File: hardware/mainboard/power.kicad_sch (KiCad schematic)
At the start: 18 parts, among them J1 Eurorack Power, U1 LD1117-3.3, U2 LM4040DBZ-10

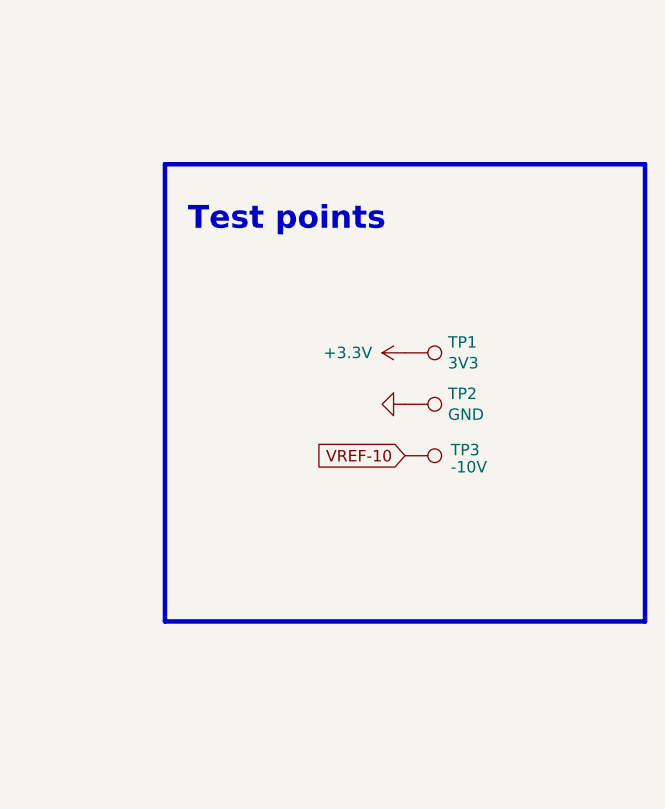
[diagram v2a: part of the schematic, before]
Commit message: A little more schematic cleanup
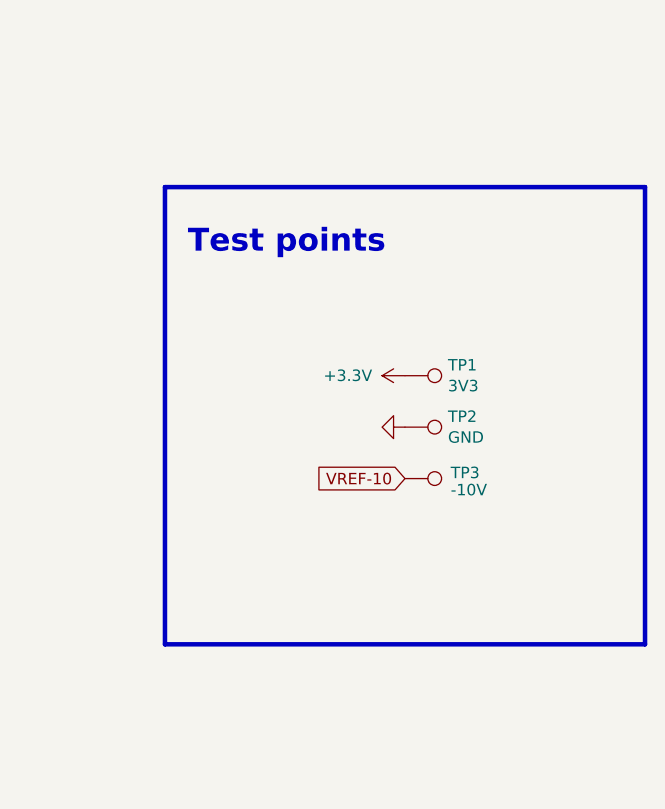
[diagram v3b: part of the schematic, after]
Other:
- moved on the sheet: TP1, TP2, TP3
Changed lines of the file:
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@@
     (stroke (width 0) (type default) (color 0 0 0 0))
   )
-  (polyline (pts (xy 208.28 114.3) (xy 208.28 165.1))
+  (polyline (pts (xy 208.28 116.84) (xy 208.28 167.64))
     (stroke (width 0.5) (type solid) (color 0 0 0 0))
   )
@@
     (stroke (width 0) (type default) (color 0 0 0 0))
   )
-  (polyline (pts (xy 208.28 165.1) (xy 261.62 165.1))
+  (polyline (pts (xy 208.28 167.64) (xy 261.62 167.64))
     (stroke (width 0.5) (type solid) (color 0 0 0 0))
   )
@@
     (stroke (width 0) (type default) (color 0 0 0 0))
   )
-  (polyline (pts (xy 208.28 114.3) (xy 261.62 114.3))
+  (polyline (pts (xy 208.28 116.84) (xy 261.62 116.84))
     (stroke (width 0.5) (type solid) (color 0 0 0 0))
   )
@@
     (stroke (width 0.5) (type solid) (color 0 0 0 0))
   )
-  (polyline (pts (xy 261.62 165.1) (xy 261.62 114.3))
+  (polyline (pts (xy 261.62 167.64) (xy 261.62 116.84))
     (stroke (width 0.5) (type solid) (color 0 0 0 0))
   )
@@
     (effects (font (size 2.54 2.54) (thickness 0.508) bold) (justify left bottom))
   )
-  (text "Test points" (at 210.82 121.92 0)
+  (text "Test points" (at 210.82 124.46 0)
     (effects (font (size 2.54 2.54) (thickness 0.508) bold) (justify left bottom))
   )
@@
     )
   )
-  (global_label "VREF-10" (shape input) (at 234.95 146.685 180) (fields_autoplaced)
+  (global_label "VREF-10" (shape input) (at 234.95 149.225 180) (fields_autoplaced)
     (effects (font (size 1.27 1.27)) (justify right))
-    (property "Intersheet References" "${INTERSHEET_REFS}" (id 0) (at 307.34 225.425 0)
+    (property "Intersheet References" "${INTERSHEET_REFS}" (id 0) (at 307.34 227.965 0)
       (effects (font (size 1.27 1.27)) hide)
     )
@@
     (pin "1")
   )
-  (symbol (lib_id "power:GND") (at 234.95 140.97 270) (unit 1)
-    (in_bom yes) (on_board yes)
-    (property "Reference" "#PWR013" (id 0) (at 228.6 140.97 0)
-      (effects (font (size 1.27 1.27)) hide)
-    )
-    (property "Value" "GND" (id 1) (at 230.5558 141.097 0)
-      (effects (font (size 1.27 1.27)) hide)
-    )
-    (property "Footprint" "" (id 2) (at 234.95 140.97 0)
-      (effects (font (size 1.27 1.27)) hide)
-    )
-    (property "Datasheet" "" (id 3) (at 234.95 140.97 0)
-      (effects (font (size 1.27 1.27)) hide)
-    )
-    (pin "1")
-  )
-  (symbol (lib_id "power:+3.3V") (at 234.95 135.255 90) (unit 1)
-    (in_bom yes) (on_board yes)
-    (property "Reference" "#PWR012" (id 0) (at 238.76 135.255 0)
-      (effects (font (size 1.27 1.27)) hide)
-    )
-    (property "Value" "+3.3V" (id 1) (at 228.6 135.255 90))
-    (property "Footprint" "" (id 2) (at 234.95 135.255 0)
-      (effects (font (size 1.27 1.27)) hide)
-    )
-    (property "Datasheet" "" (id 3) (at 234.95 135.255 0)
+  (symbol (lib_id "power:GND") (at 234.95 143.51 270) (unit 1)
+    (in_bom yes) (on_board yes)
+    (property "Reference" "#PWR013" (id 0) (at 228.6 143.51 0)
+      (effects (font (size 1.27 1.27)) hide)
+    )
+    (property "Value" "GND" (id 1) (at 230.5558 143.637 0)
+      (effects (font (size 1.27 1.27)) hide)
+    )
+    (property "Footprint" "" (id 2) (at 234.95 143.51 0)
+      (effects (font (size 1.27 1.27)) hide)
+    )
+    (property "Datasheet" "" (id 3) (at 234.95 143.51 0)
+      (effects (font (size 1.27 1.27)) hide)
+    )
+    (pin "1")
+  )
+  (symbol (lib_id "power:+3.3V") (at 234.95 137.795 90) (unit 1)
+    (in_bom yes) (on_board yes)
+    (property "Reference" "#PWR012" (id 0) (at 238.76 137.795 0)
+      (effects (font (size 1.27 1.27)) hide)
+    )
+    (property "Value" "+3.3V" (id 1) (at 228.6 137.795 90))
+    (property "Footprint" "" (id 2) (at 234.95 137.795 0)
+      (effects (font (size 1.27 1.27)) hide)
+    )
+    (property "Datasheet" "" (id 3) (at 234.95 137.795 0)
       (effects (font (size 1.27 1.27)) hide)
     )
@@
     (pin "1")
   )
-  (symbol (lib_id "Connector:TestPoint") (at 234.95 146.685 270) (unit 1)
-    (in_bom yes) (on_board yes)
-    (property "Reference" "TP3" (id 0) (at 240.03 146.05 90)
-      (effects (font (size 1.27 1.27)) (justify left))
-    )
-    (property "Value" "-10V" (id 1) (at 240.03 147.955 90)
-      (effects (font (size 1.27 1.27)) (justify left))
-    )
-    (property "Footprint" "TestPoint:TestPoint_Pad_D1.0mm" (id 2) (at 234.95 151.765 0)
-      (effects (font (size 1.27 1.27)) hide)
-    )
-    (property "Datasheet" "~" (id 3) (at 234.95 151.765 0)
-      (effects (font (size 1.27 1.27)) hide)
-    )
-    (property "dnp" "1" (id 4) (at 234.95 146.685 0)
-      (effects (font (size 1.27 1.27)) hide)
-    )
-    (property "finalized" "n/a" (id 5) (at 234.95 146.685 0)
-      (effects (font (size 1.27 1.27)) hide)
-    )
-    (pin "1")
-  )
-  (symbol (lib_id "Connector:TestPoint") (at 234.95 135.255 270) (unit 1)
-    (in_bom yes) (on_board yes)
-    (property "Reference" "TP1" (id 0) (at 239.7252 134.0866 90)
-      (effects (font (size 1.27 1.27)) (justify left))
-    )
-    (property "Value" "3V3" (id 1) (at 239.7252 136.398 90)
-      (effects (font (size 1.27 1.27)) (justify left))
-    )
-    (property "Footprint" "TestPoint:TestPoint_Pad_D1.0mm" (id 2) (at 234.95 140.335 0)
-      (effects (font (size 1.27 1.27)) hide)
-    )
-    (property "Datasheet" "~" (id 3) (at 234.95 140.335 0)
-      (effects (font (size 1.27 1.27)) hide)
-    )
-    (property "dnp" "1" (id 4) (at 234.95 135.255 0)
-      (effects (font (size 1.27 1.27)) hide)
-    )
-    (property "finalized" "n/a" (id 5) (at 234.95 135.255 0)
+  (symbol (lib_id "Connector:TestPoint") (at 234.95 149.225 270) (unit 1)
+    (in_bom yes) (on_board yes)
+    (property "Reference" "TP3" (id 0) (at 240.03 148.59 90)
+      (effects (font (size 1.27 1.27)) (justify left))
+    )
+    (property "Value" "-10V" (id 1) (at 240.03 150.495 90)
+      (effects (font (size 1.27 1.27)) (justify left))
+    )
+    (property "Footprint" "TestPoint:TestPoint_Pad_D1.0mm" (id 2) (at 234.95 154.305 0)
+      (effects (font (size 1.27 1.27)) hide)
+    )
+    (property "Datasheet" "~" (id 3) (at 234.95 154.305 0)
+      (effects (font (size 1.27 1.27)) hide)
+    )
+    (property "dnp" "1" (id 4) (at 234.95 149.225 0)
+      (effects (font (size 1.27 1.27)) hide)
+    )
+    (property "finalized" "n/a" (id 5) (at 234.95 149.225 0)
+      (effects (font (size 1.27 1.27)) hide)
+    )
+    (pin "1")
+  )
+  (symbol (lib_id "Connector:TestPoint") (at 234.95 137.795 270) (unit 1)
+    (in_bom yes) (on_board yes)
+    (property "Reference" "TP1" (id 0) (at 239.7252 136.6266 90)
+      (effects (font (size 1.27 1.27)) (justify left))
+    )
+    (property "Value" "3V3" (id 1) (at 239.7252 138.938 90)
+      (effects (font (size 1.27 1.27)) (justify left))
+    )
+    (property "Footprint" "TestPoint:TestPoint_Pad_D1.0mm" (id 2) (at 234.95 142.875 0)
+      (effects (font (size 1.27 1.27)) hide)
+    )
+    (property "Datasheet" "~" (id 3) (at 234.95 142.875 0)
+      (effects (font (size 1.27 1.27)) hide)
+    )
+    (property "dnp" "1" (id 4) (at 234.95 137.795 0)
+      (effects (font (size 1.27 1.27)) hide)
+    )
+    (property "finalized" "n/a" (id 5) (at 234.95 137.795 0)
       (effects (font (size 1.27 1.27)) hide)
     )
@@
     (pin "2")
   )
-  (symbol (lib_id "Connector:TestPoint") (at 234.95 140.97 270) (unit 1)
-    (in_bom yes) (on_board yes)
-    (property "Reference" "TP2" (id 0) (at 239.7252 139.8016 90)
-      (effects (font (size 1.27 1.27)) (justify left))
-    )
-    (property "Value" "GND" (id 1) (at 239.7252 142.113 90)
-      (effects (font (size 1.27 1.27)) (justify left))
-    )
-    (property "Footprint" "TestPoint:TestPoint_Pad_D1.0mm" (id 2) (at 234.95 146.05 0)
-      (effects (font (size 1.27 1.27)) hide)
-    )
-    (property "Datasheet" "~" (id 3) (at 234.95 146.05 0)
-      (effects (font (size 1.27 1.27)) hide)
-    )
-    (property "dnp" "1" (id 4) (at 234.95 140.97 0)
-      (effects (font (size 1.27 1.27)) hide)
-    )
-    (property "finalized" "n/a" (id 5) (at 234.95 140.97 0)
-      (effects (font (size 1.27 1.27)) hide)
-    )
+  (symbol (lib_id "Connector:TestPoint") (at 234.95 143.51 270) (unit 1)
+    (in_bom yes) (on_board yes)
+    (property "Reference" "TP2" (id 0) (at 239.7252 142.3416 90)
+      (effects (font (size 1.27 1.27)) (justify left))
+    )
+    (property "Value" "GND" (id 1) (at 239.7252 144.653 90)
+      (effects (font (size 1.27 1.27)) (justify left))
+    )
+    (property "Footprint" "TestPoint:TestPoint_Pad_D1.0mm" (id 2) (at 234.95 148.59 0)
+      (effects (font (size 1.27 1.27)) hide)
+    )
+    (property "Datasheet" "~" (id 3) (at 234.95 148.59 0)
+      (effects (font (size 1.27 1.27)) hide)
+    )
+    (property "dnp" "1" (id 4) (at 234.95 143.51 0)
+      (effects (font (size 1.27 1.27)) hide)
+    )
+    (property "finalized" "n/a" (id 5) (at 234.95 143.51 0)
+      (effects (font (size 1.27 1.27)) hide)
+    )

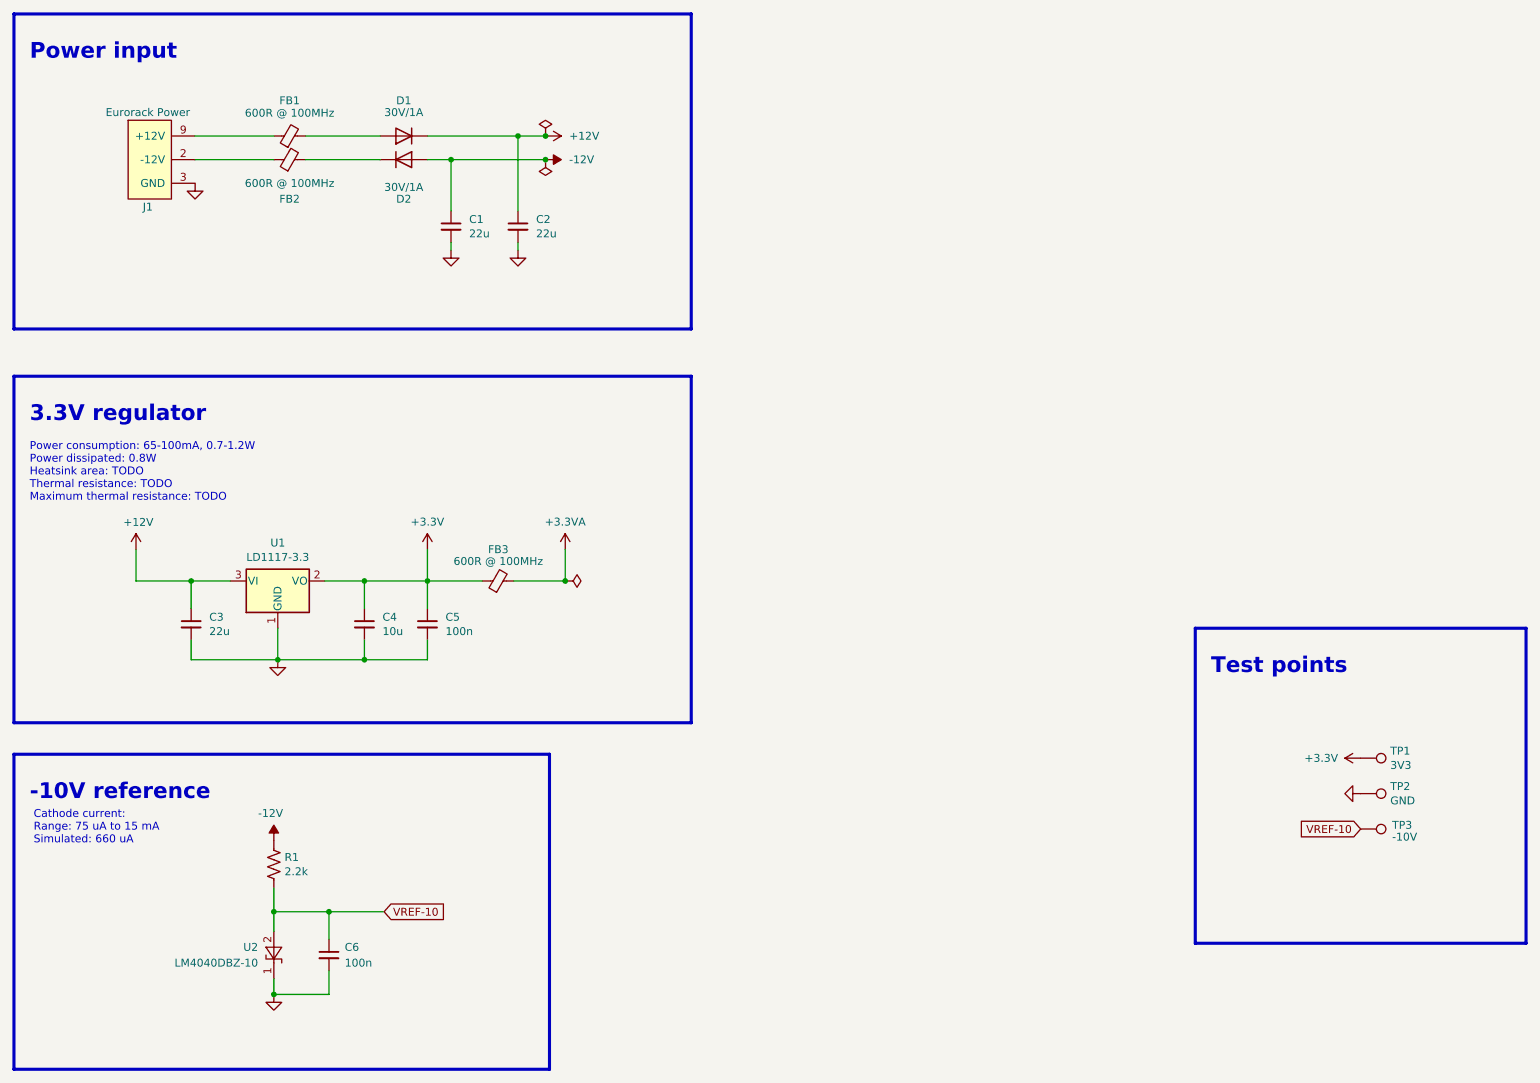
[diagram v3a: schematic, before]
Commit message: * Added versions strapping pins * Added VBUS power * Filled out regulator thermal calculations
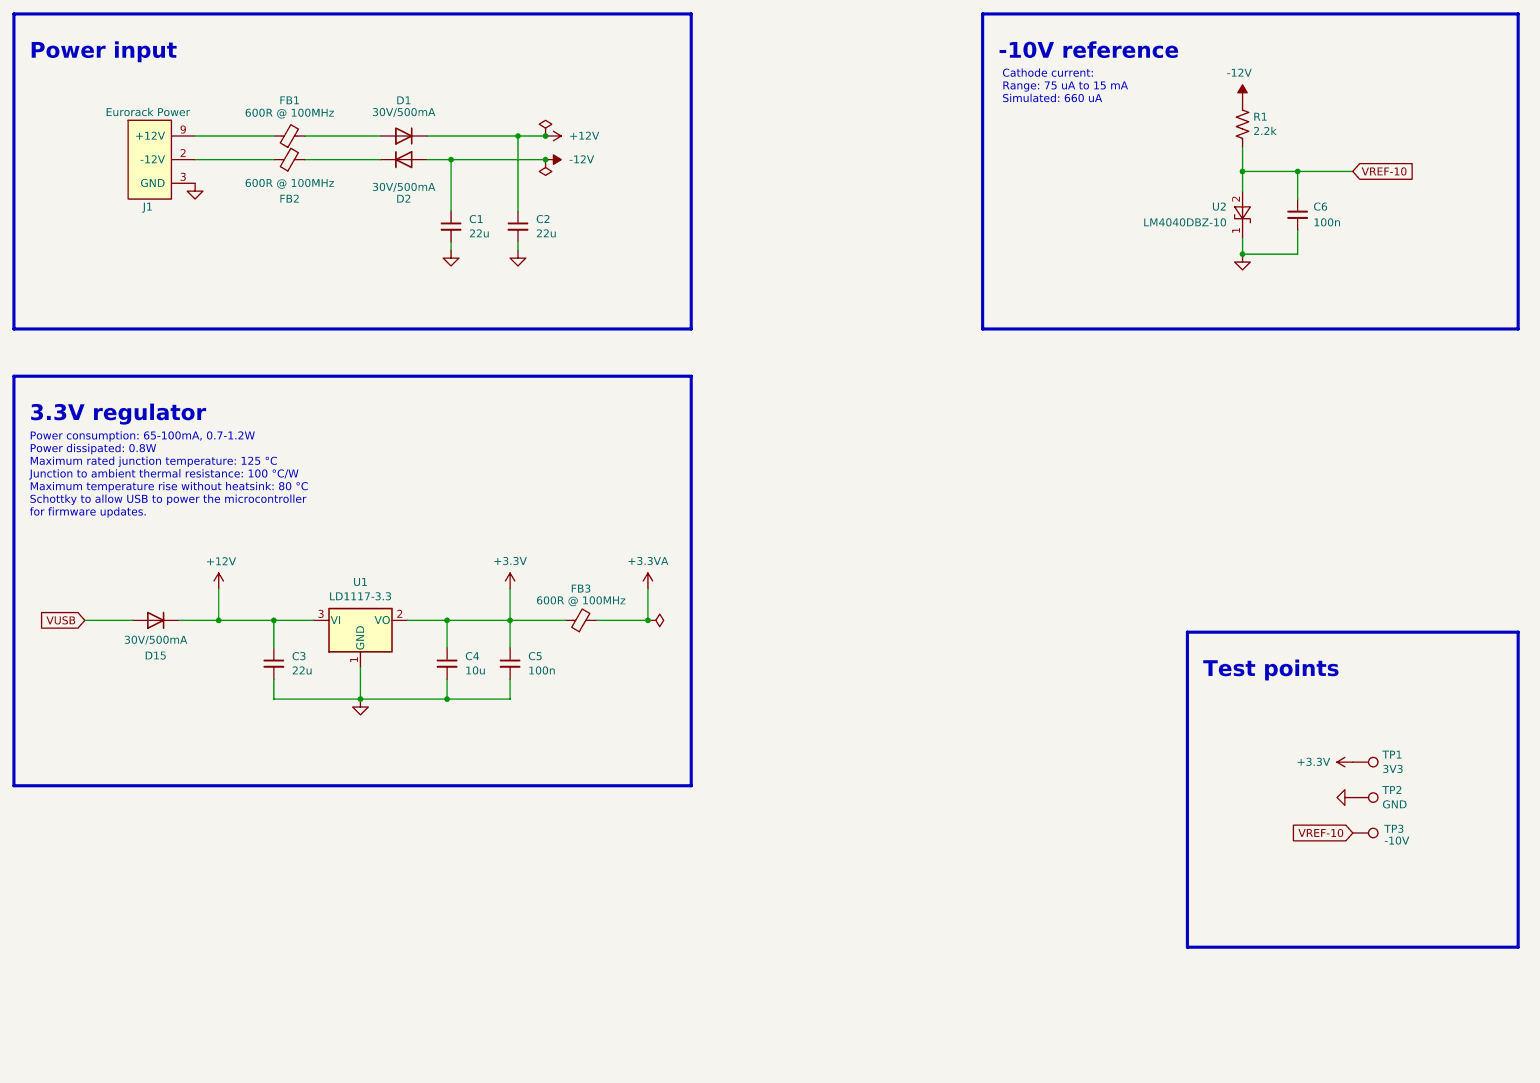
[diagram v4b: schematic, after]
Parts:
- added D15: 30V/500mA, winterbloom:D_SOD-123, symbol Device:D
- D1: value 30V/1A -> 30V/500mA
- D2: value 30V/1A -> 30V/500mA
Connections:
- net +12V: now also D15.1 (K)
- new net VUSB: D15.2 (A)
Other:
- note added: "Power consumption: 65-100mA, 0.7-1.2W Power dissipated: 0.8W Maximum rated junction temperature: 125 °C Junction to ambient thermal resistance: 100 °C/W Maximum temperature rise without heatsink: 80 °C Schottky to allow USB to power the microcontroller for firmware updates."
- note removed: "Power consumption: 65-100mA, 0.7-1.2W Power dissipated: 0.8W Heatsink area: TODO Thermal resistance: TODO Maximum thermal resistance: TODO"
- moved on the sheet: C3, C4, C5, C6, FB3, R1, TP1, TP2, TP3, U1, U2

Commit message: Update some MPNs
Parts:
- R1: mpn (none) -> ERJ-2RKF2201X
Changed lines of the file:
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@@
       (effects (font (size 1.27 1.27)) hide)
     )
-    (property "mpn" "" (id 5) (at 215.9 35.56 0)
+    (property "mpn" "ERJ-2RKF2201X" (id 5) (at 215.9 35.56 0)
       (effects (font (size 1.27 1.27)) hide)
     )
